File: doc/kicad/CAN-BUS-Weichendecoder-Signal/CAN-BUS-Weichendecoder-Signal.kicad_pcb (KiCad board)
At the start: 2 copper layers, 151.1 x 124.5 mm, 26 parts, among them J1 Conn_01x04_Male, J1001 Wago 250-1406, J11 250-1406, J12 Wago 250-1406, J13 Wago 250-1406, J14 Wago 250-1406, J15 Wago 250-1406, J21 Conn_01x06, J22 Conn_01x06, U1 PCF8574, U2 PCF8574, U3 PCF8574, U4 PCF8574, U5 ULN2803A, U6 ULN2803A, U7 ULN2803A, U8 ULN2803A

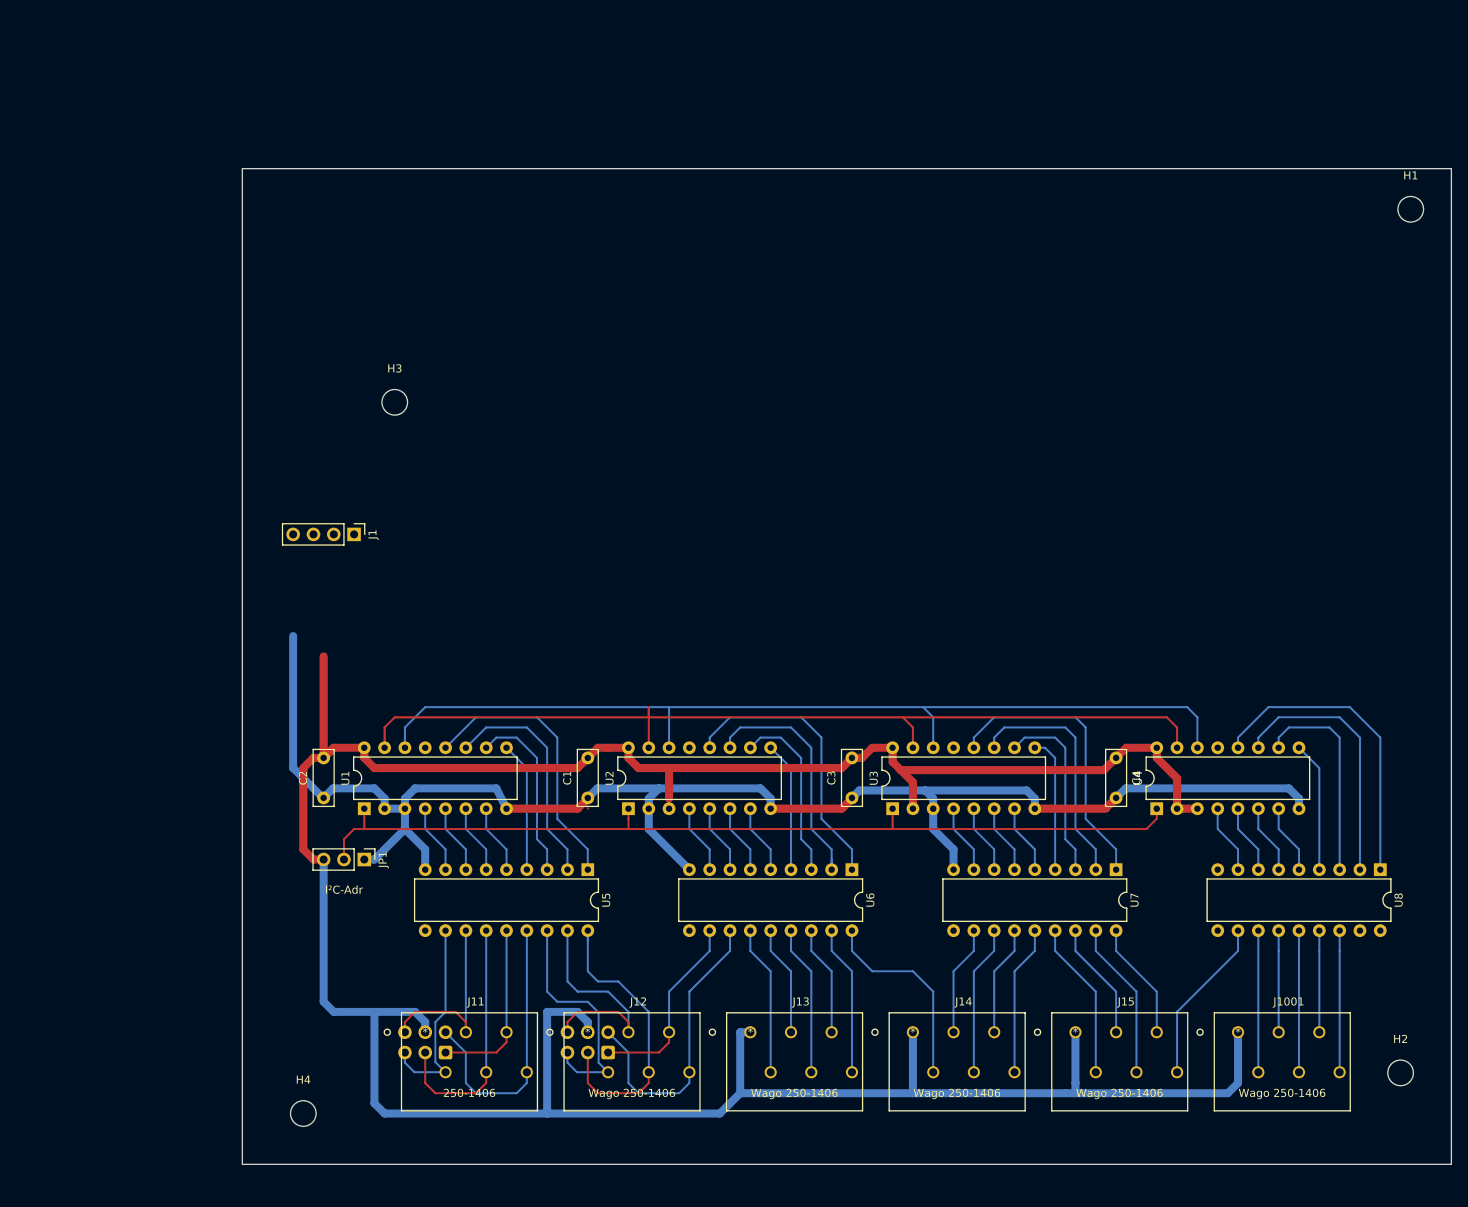
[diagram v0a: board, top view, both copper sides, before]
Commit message: RJ12 hinzugefügt
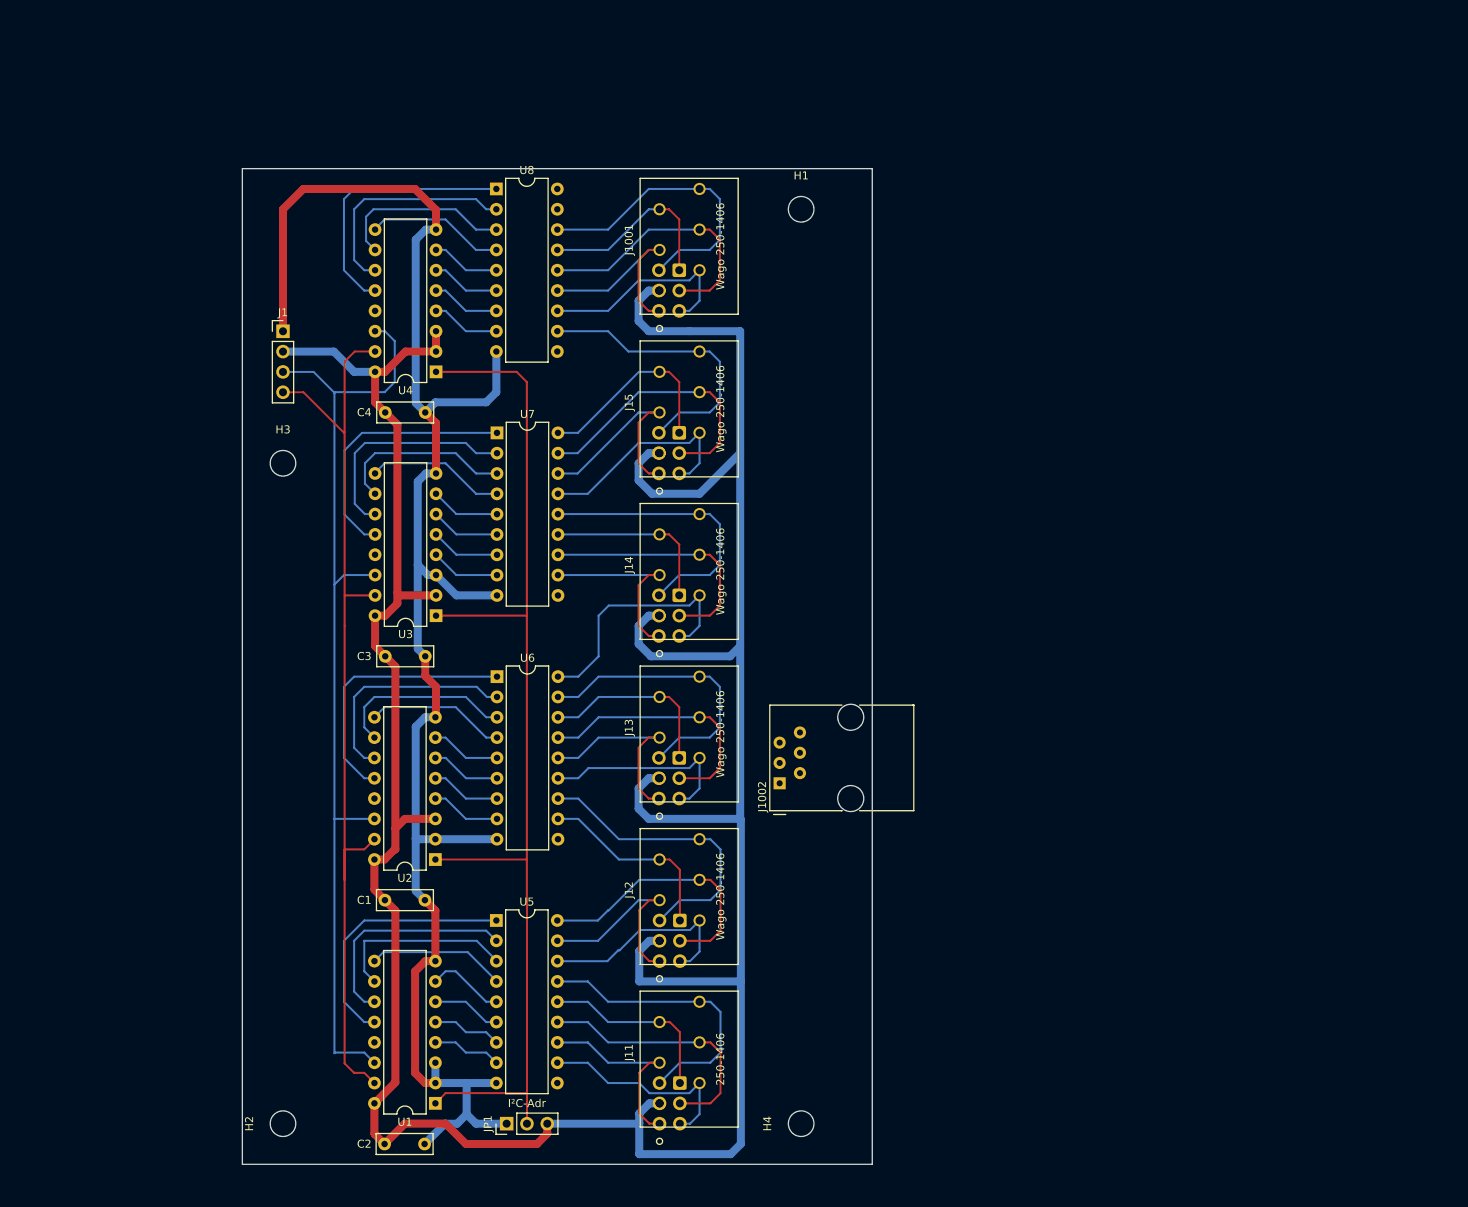
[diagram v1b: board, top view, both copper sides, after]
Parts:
- added J1002: RJ12, Connector_RJ:RJ12_Amphenol_54601, F.Cu at (128.1, 128.9)
- added J23: Conn_01x06, Connector_IDC:IDC-Header_2x03_P2.54mm_Vertical, B.Cu at (115.6, 125.7)
- added J24: Conn_01x06, Connector_IDC:IDC-Header_2x03_P2.54mm_Vertical, B.Cu at (115.6, 105.4)
- added J25: Conn_01x06, Connector_IDC:IDC-Header_2x03_P2.54mm_Vertical, B.Cu at (115.6, 85.1)
- added J26: Conn_01x06, Connector_IDC:IDC-Header_2x03_P2.54mm_Vertical, B.Cu at (115.6, 64.8)
- J21, J22: footprint Connectors_IDC:IDC-Header_2x03_P2.54mm_Vertical -> Connector_IDC:IDC-Header_2x03_P2.54mm_Vertical
- moved H2 139.8 mm to (66.0, 171.4), turned to 90 degrees
- moved U8 139.5 mm to (92.7, 54.6), turned to 0 degrees
- moved J1001 117.6 mm to (113.1, 67.3), turned to 90 degrees
- moved U4 105.3 mm to (85.2, 77.5), turned to 180 degrees
- moved C4 101.1 mm to (78.8, 82.5), turned to 0 degrees
- moved U7 94.7 mm to (92.8, 85.1), turned to 0 degrees
- moved J15 89.1 mm to (113.1, 87.6), turned to 90 degrees
- moved H1 76.2 mm to (130.8, 57.1)
- moved H4 62.2 mm to (130.8, 171.4), turned to 90 degrees
- moved U3 62.0 mm to (85.2, 108.0), turned to 180 degrees
- moved J14 60.9 mm to (113.1, 108.0), turned to 90 degrees
- moved C3 59.7 mm to (78.8, 113.0), turned to 0 degrees
- moved U6 50.5 mm to (92.8, 115.6), turned to 0 degrees
- moved C2 48.9 mm to (78.7, 174.0), turned to 0 degrees
- moved U1 37.9 mm to (85.1, 168.9), turned to 180 degrees
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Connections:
- J1 pad 1: +5V -> GND
- J1 pad 2: Net-(J1-Pad2) -> +5V
- J1 pad 4: GND -> Net-(J1-Pad4)
- U1 pad 14: Net-(J1-Pad2) -> Net-(J1-Pad3)
- U1 pad 15: Net-(J1-Pad3) -> Net-(J1-Pad4)
- U2 pad 14: Net-(J1-Pad2) -> Net-(J1-Pad3)
- U2 pad 15: Net-(J1-Pad3) -> Net-(J1-Pad4)
- U3 pad 14: Net-(J1-Pad2) -> Net-(J1-Pad3)
- U3 pad 15: Net-(J1-Pad3) -> Net-(J1-Pad4)
- U4 pad 14: Net-(J1-Pad2) -> Net-(J1-Pad3)
- U4 pad 15: Net-(J1-Pad3) -> Net-(J1-Pad4)
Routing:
- net Net-(J1-Pad4): track 0.00 -> 118.5 mm
- net Net-(J1-Pad2): track 117.7 -> 0.00 mm
- net Net-(JP1-Pad2): track 114.1 -> 139.3 mm
- net +5V: track 370.9 -> 395.5 mm, vias 1 -> 0
- net GND: track 197.6 -> 220.7 mm
- net Net-(J1001-Pad6): track 17.7 -> 37.2 mm
- net Net-(J13-Pad6): track 18.8 -> 36.1 mm
- net Net-(J14-Pad6): track 18.8 -> 35.0 mm
- net Net-(J1001-Pad4): track 17.7 -> 33.6 mm
- net Net-(J15-Pad6): track 20.9 -> 36.2 mm
- net Net-(J15-Pad4): track 19.8 -> 34.6 mm
- net Net-(J13-Pad4): track 18.8 -> 32.5 mm
- net Net-(J1001-Pad3): track 12.7 -> 26.2 mm
- net Net-(J14-Pad4): track 18.8 -> 31.5 mm
- net Net-(J15-Pad3): track 14.8 -> 27.2 mm
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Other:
- board size 151.1 x 124.5 mm -> 78.7 x 124.5 mm

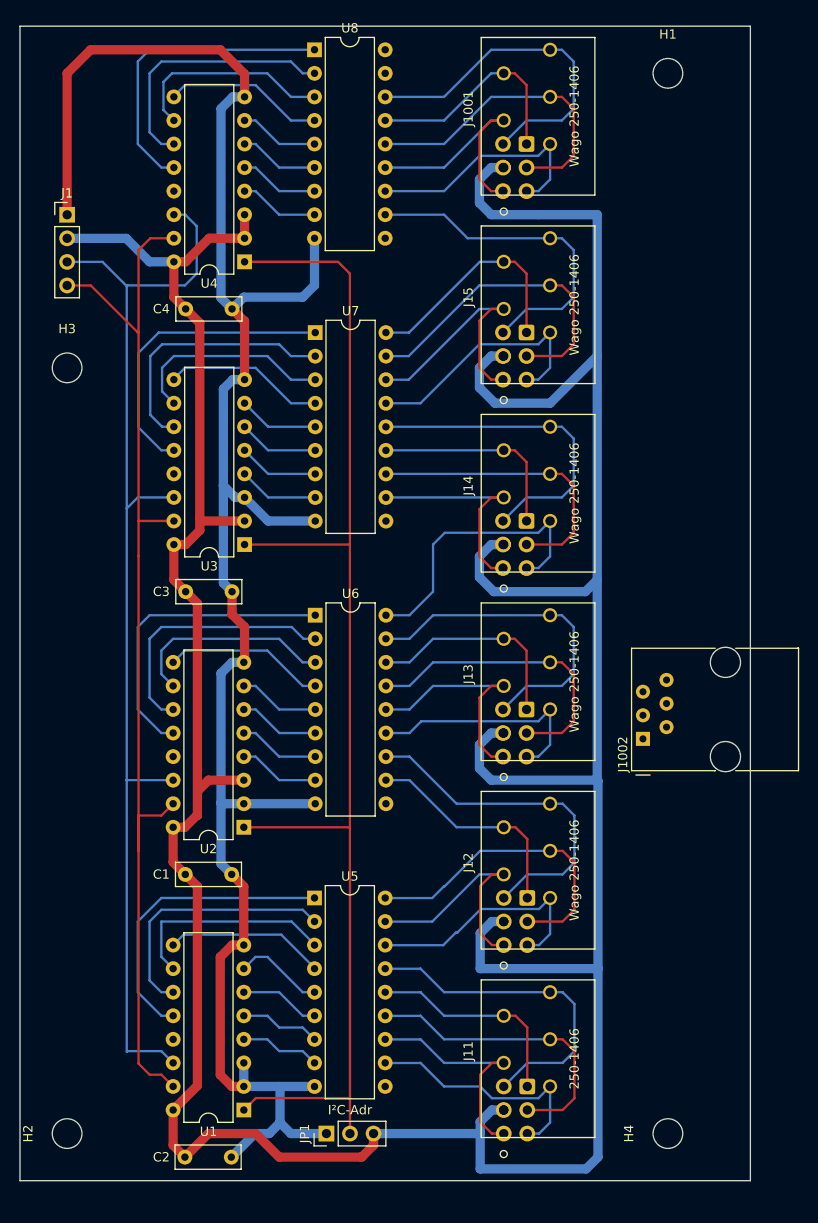
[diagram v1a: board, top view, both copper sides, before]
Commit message: Ausgänge in zwei Blöcke aufgetreilt, Ausgangsspannung kann extern eingespeist werden
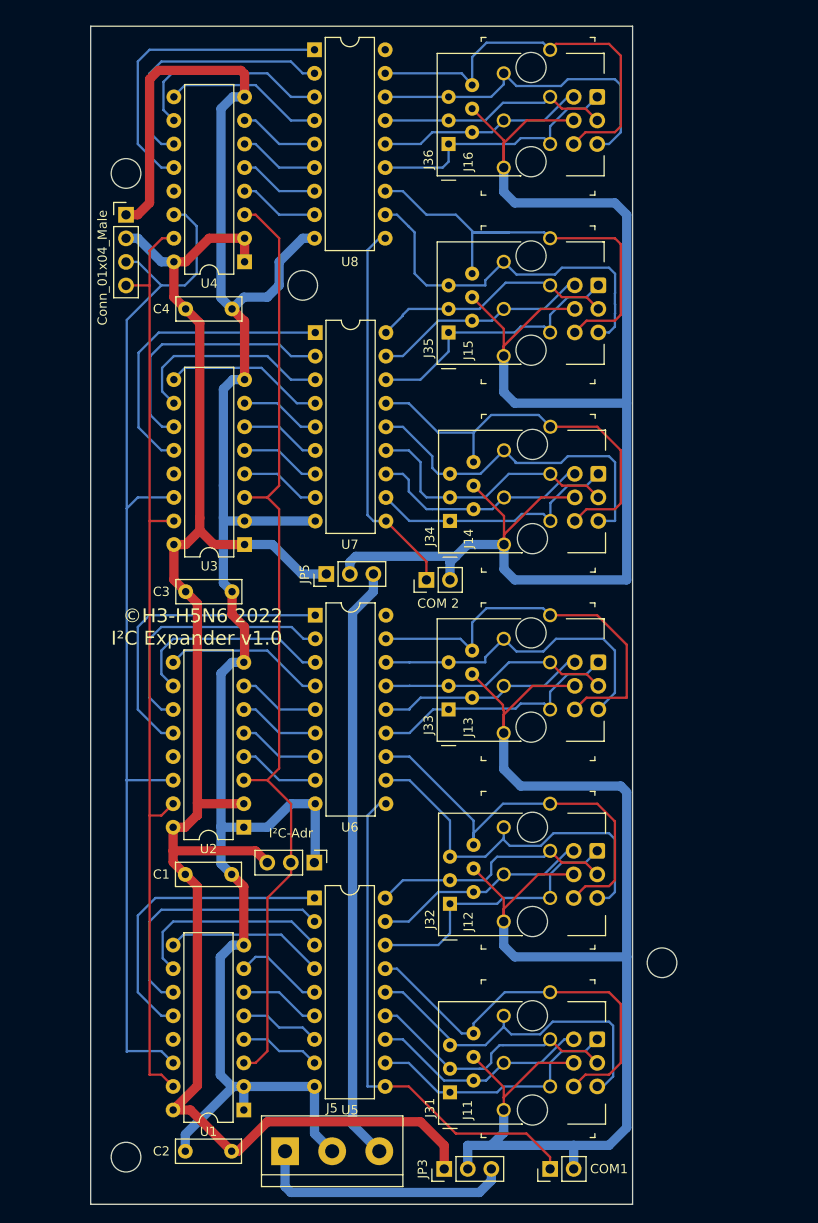
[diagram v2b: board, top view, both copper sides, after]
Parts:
- added J31: RJ12, Wago:RJ12_Amphenol_54601_Light, F.Cu at (107.3, 167.0)
- added J32: RJ12, Wago:RJ12_Amphenol_54601_Light, F.Cu at (107.3, 146.7)
- added J34: RJ12, Wago:RJ12_Amphenol_54601_Light, F.Cu at (107.3, 105.4)
- added J35: RJ12, Wago:RJ12_Amphenol_54601_Light, F.Cu at (107.2, 85.1)
- added J36: RJ12, Wago:RJ12_Amphenol_54601_Light, F.Cu at (107.2, 64.8)
- added J5: Conn_01x03, TerminalBlock:TerminalBlock_bornier-3_P5.08mm, F.Cu at (89.5, 173.4)
- added JP2: COM1, Connector_PinHeader_2.54mm:PinHeader_1x02_P2.54mm_Vertical, F.Cu at (118.1, 175.3)
- added JP3: Jumper_3_Bridged12, Connector_PinHeader_2.54mm:PinHeader_1x03_P2.54mm_Vertical, F.Cu at (106.7, 175.3)
- added JP4: COM 2, Connector_PinHeader_2.54mm:PinHeader_1x02_P2.54mm_Vertical, F.Cu at (104.8, 111.8)
- added JP5: Jumper_3_Bridged12, Connector_PinHeader_2.54mm:PinHeader_1x03_P2.54mm_Vertical, F.Cu at (94.0, 111.1)
- J11, J12, J13, J14, J15: footprint Wago:CONN_250-1406_WAG -> Wago:CONN_250-1406_WAG_Light
- J16: renamed from J1001; footprint Wago:CONN_250-1406_WAG -> Wago:CONN_250-1406_WAG_Light
- J21, J22, J23, J24, J25, J26: footprint Connector_IDC:IDC-Header_2x03_P2.54mm_Vertical -> Wago:IDC-Header_2x03_P2.54mm_Vertical_Light
- J33: renamed from J1002; footprint Connector_RJ:RJ12_Amphenol_54601 -> Wago:RJ12_Amphenol_54601_Light
- moved H1 45.5 mm to (91.4, 80.0)
- moved JP1 29.2 mm to (92.7, 142.2), turned to -90 degrees
- moved H3 21.9 mm to (72.4, 67.9)
- moved J33 21.2 mm to (107.2, 125.7)
- moved H4 18.4 mm to (130.2, 153.0)
- moved J23 9.26 mm to (123.3, 120.6)
- moved J25 9.26 mm to (123.3, 80.0)
- moved J24 9.26 mm to (123.3, 100.3)
- moved J26 9.16 mm to (123.2, 59.7)
- moved J21 9.09 mm to (123.2, 161.3)
- moved J22 9.09 mm to (123.2, 141.0)
- moved H2 6.84 mm to (72.4, 174.0)
- moved J1 6.35 mm to (72.4, 72.4)
- moved C2 5.08 mm to (83.8, 173.4), turned to 180 degrees
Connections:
- J11 pad 1: +5V -> Net-(J11-Pad1)
- J12 pad 1: +5V -> Net-(J11-Pad1)
- J13 pad 1: +5V -> Net-(J11-Pad1)
- J14 pad 1: +5V -> Net-(J14-Pad1)
- J15 pad 1: +5V -> Net-(J14-Pad1)
- J16 pad 1: +5V -> Net-(J14-Pad1)
- J16 pad 2: Net-(J1001-Pad2) -> Net-(J16-Pad2)
- J16 pad 3: Net-(J1001-Pad3) -> Net-(J16-Pad3)
- J16 pad 4: Net-(J1001-Pad4) -> Net-(J16-Pad4)
- J16 pad 5: Net-(J1001-Pad5) -> Net-(J16-Pad5)
- J16 pad 6: Net-(J1001-Pad6) -> Net-(J16-Pad6)
- J21 pad 1: Net-(J11-Pad5) -> Net-(J11-Pad2)
- J21 pad 2: Net-(J11-Pad6) -> Net-(J11-Pad3)
- J21 pad 4: +5V -> Net-(J11-Pad1)
- J21 pad 5: Net-(J11-Pad2) -> Net-(J11-Pad5)
- J21 pad 6: Net-(J11-Pad3) -> Net-(J11-Pad6)
- J22 pad 1: Net-(J12-Pad5) -> Net-(J12-Pad2)
- J22 pad 2: Net-(J12-Pad6) -> Net-(J12-Pad3)
- J22 pad 4: +5V -> Net-(J11-Pad1)
- J22 pad 5: Net-(J12-Pad2) -> Net-(J12-Pad5)
- J22 pad 6: Net-(J12-Pad3) -> Net-(J12-Pad6)
- J23 pad 1: Net-(J13-Pad5) -> Net-(J13-Pad2)
- J23 pad 2: Net-(J13-Pad6) -> Net-(J13-Pad3)
- J23 pad 4: +5V -> Net-(J11-Pad1)
- J23 pad 5: Net-(J13-Pad2) -> Net-(J13-Pad5)
- J23 pad 6: Net-(J13-Pad3) -> Net-(J13-Pad6)
- J24 pad 1: Net-(J14-Pad5) -> Net-(J14-Pad2)
- J24 pad 2: Net-(J14-Pad6) -> Net-(J14-Pad3)
- J24 pad 4: +5V -> Net-(J14-Pad1)
- J24 pad 5: Net-(J14-Pad2) -> Net-(J14-Pad5)
- J24 pad 6: Net-(J14-Pad3) -> Net-(J14-Pad6)
- J25 pad 1: Net-(J15-Pad5) -> Net-(J15-Pad2)
- J25 pad 2: Net-(J15-Pad6) -> Net-(J15-Pad3)
- J25 pad 4: +5V -> Net-(J14-Pad1)
- J25 pad 5: Net-(J15-Pad2) -> Net-(J15-Pad5)
- J25 pad 6: Net-(J15-Pad3) -> Net-(J15-Pad6)
- J26 pad 1: Net-(J1001-Pad5) -> Net-(J16-Pad2)
- J26 pad 2: Net-(J1001-Pad6) -> Net-(J16-Pad3)
- J26 pad 3: Net-(J1001-Pad4) -> Net-(J16-Pad4)
- J26 pad 4: +5V -> Net-(J14-Pad1)
- J26 pad 5: Net-(J1001-Pad2) -> Net-(J16-Pad5)
- J26 pad 6: Net-(J1001-Pad3) -> Net-(J16-Pad6)
- J33 pad 1: unconnected-(J1002-Pad1) -> Net-(J13-Pad2)
- J33 pad 2: unconnected-(J1002-Pad2) -> Net-(J13-Pad3)
- J33 pad 3: unconnected-(J1002-Pad3) -> Net-(J13-Pad4)
- J33 pad 4: unconnected-(J1002-Pad4) -> Net-(J11-Pad1)
- J33 pad 5: unconnected-(J1002-Pad5) -> Net-(J13-Pad5)
- J33 pad 6: unconnected-(J1002-Pad6) -> Net-(J13-Pad6)
- JP1 pad 2: Net-(JP1-Pad2) -> Net-(U3-Pad3)
- U1 pad 1: Net-(JP1-Pad2) -> GND
- U1 pad 3: GND -> Net-(U3-Pad3)
- U2 pad 1: Net-(JP1-Pad2) -> GND
- U2 pad 2: GND -> +5V
- U2 pad 3: +5V -> Net-(U3-Pad3)
- U3 pad 1: Net-(JP1-Pad2) -> +5V
- U3 pad 2: +5V -> GND
- U3 pad 3: GND -> Net-(U3-Pad3)
- U4 pad 1: Net-(JP1-Pad2) -> +5V
- U4 pad 3: +5V -> Net-(U3-Pad3)
- U5 pad 10: unconnected-(U5-Pad10) -> Net-(JP2-Pad1)
- U6 pad 10: unconnected-(U6-Pad10) -> Net-(JP2-Pad1)
- U6 pad 18: Net-(J14-Pad2) -> unconnected-(U6-Pad18)
- U7 pad 10: unconnected-(U7-Pad10) -> Net-(JP4-Pad1)
- U7 pad 11: Net-(J14-Pad3) -> Net-(J14-Pad2)
- U7 pad 12: Net-(J14-Pad4) -> Net-(J14-Pad3)
- U7 pad 13: Net-(J14-Pad5) -> Net-(J14-Pad4)
- U7 pad 14: Net-(J14-Pad6) -> Net-(J14-Pad5)
- U7 pad 15: Net-(J15-Pad2) -> Net-(J14-Pad6)
- U7 pad 16: Net-(J15-Pad3) -> Net-(J15-Pad2)
- U7 pad 17: Net-(J15-Pad4) -> Net-(J15-Pad3)
- U7 pad 18: Net-(J15-Pad5) -> Net-(J15-Pad4)
- U8 pad 10: unconnected-(U8-Pad10) -> Net-(JP4-Pad1)
- U8 pad 11: Net-(J15-Pad6) -> Net-(J15-Pad5)
- U8 pad 12: Net-(J1001-Pad2) -> Net-(J15-Pad6)
- U8 pad 13: Net-(J1001-Pad3) -> Net-(J16-Pad2)
- U8 pad 14: Net-(J1001-Pad4) -> Net-(J16-Pad3)
- U8 pad 15: Net-(J1001-Pad5) -> Net-(J16-Pad4)
- U8 pad 16: Net-(J1001-Pad6) -> Net-(J16-Pad5)
- U8 pad 17: unconnected-(U8-Pad17) -> Net-(J16-Pad6)
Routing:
- net +5V: track 395.5 -> 184.3 mm
- net Net-(J14-Pad1): track 0.00 -> 166.9 mm
- net Net-(J11-Pad1): track 0.00 -> 150.4 mm
- net Net-(JP1-Pad2): track 139.3 -> 0.00 mm
- net Net-(U3-Pad3): track 0.00 -> 104.2 mm
- net Net-(J5-Pad3): track 0.00 -> 64.4 mm
- net Net-(JP2-Pad1): track 0.00 -> 55.8 mm
- net Net-(J16-Pad6): track 0.00 -> 44.2 mm
- net Net-(JP4-Pad1): track 0.00 -> 41.4 mm
- net Net-(J1001-Pad6): track 37.2 -> 0.00 mm
- net Net-(J16-Pad5): track 0.00 -> 36.4 mm
- net Net-(J1001-Pad4): track 33.6 -> 0.00 mm
- net Net-(J16-Pad2): track 0.00 -> 28.8 mm
- net Net-(J5-Pad1): track 0.00 -> 28.1 mm
- net Net-(J1001-Pad2): track 26.8 -> 0.00 mm
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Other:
- board size 78.7 x 124.5 mm -> 58.4 x 127 mm
- board text added: "©H3-H5N6 2022 I²C Expander v1.0"
